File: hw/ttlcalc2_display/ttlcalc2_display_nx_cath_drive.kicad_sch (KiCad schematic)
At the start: 23 parts, among them Q16 MPSA42, Q17 MPSA42, Q18 MPSA42, Q29 MPSA42, Q30 MPSA42, Q31 MPSA42, Q6 MPSA42, Q7 MPSA42, Q8 MPSA42, Q9 MPSA42, U12 74LS42, U7 74LS04, U8 74LS04

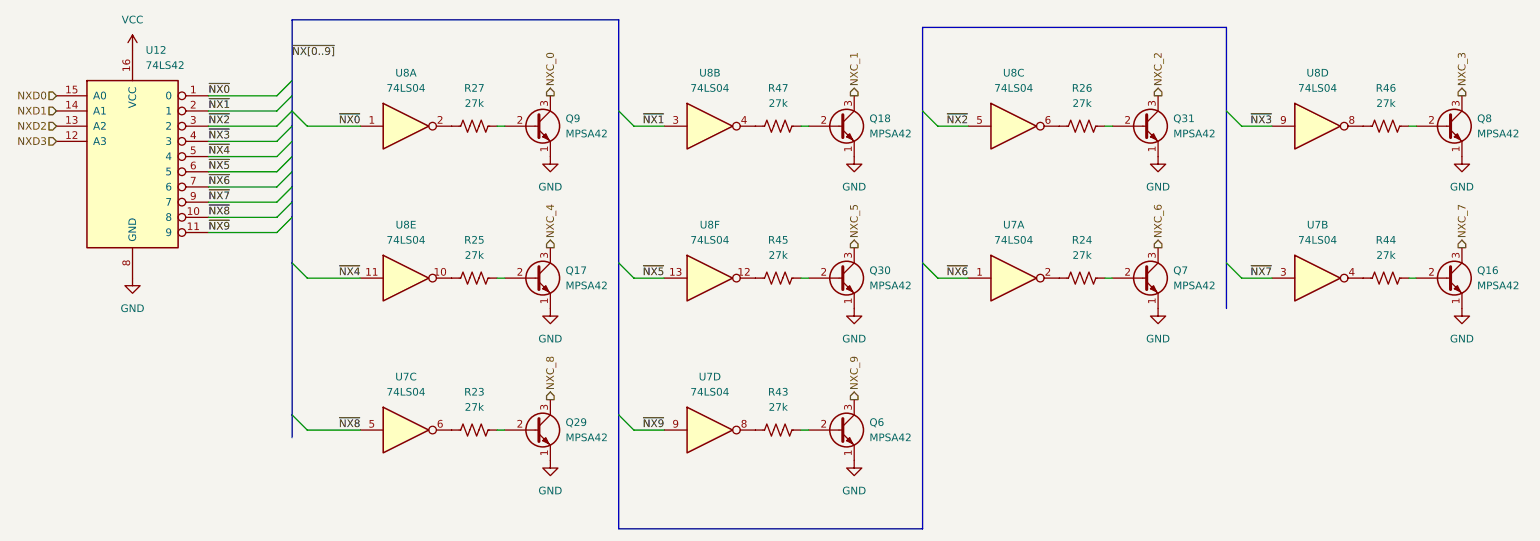
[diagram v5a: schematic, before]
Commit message: Convert to KiCad 9.0
Convert to KiCad 9.0 format
Tweak silkscreen to fix DRC errors introduced by updated footprints
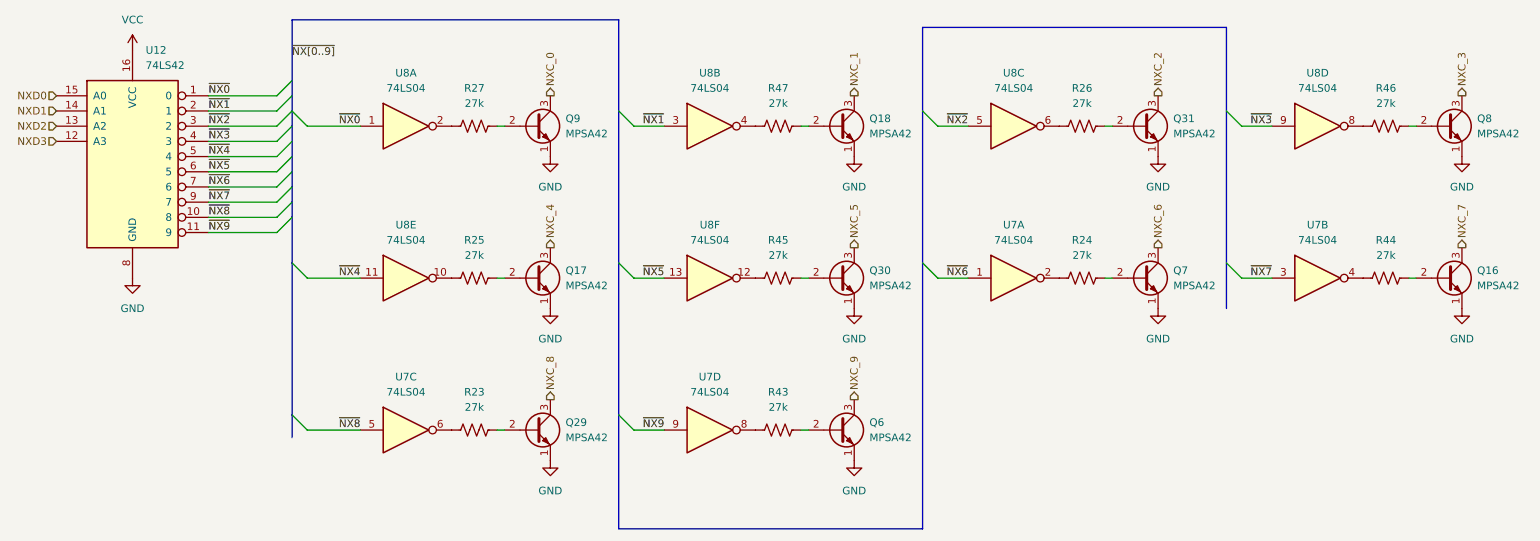
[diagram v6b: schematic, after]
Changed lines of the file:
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@@
 (kicad_sch
-	(version 20231120)
+	(version 20250114)
 	(generator "eeschema")
-	(generator_version "8.0")
+	(generator_version "9.0")
 	(paper "USLetter")
 	(title_block
@@
 	(label "~{NX4}"
 		(at 71.12 66.04 180)
-		(fields_autoplaced yes)
 		(effects
 			(font
@@
 	(label "~{NX7}"
 		(at 45.72 53.34 0)
-		(fields_autoplaced yes)
 		(effects
 			(font
@@
 	(label "~{NX1}"
 		(at 45.72 38.1 0)
-		(fields_autoplaced yes)
 		(effects
 			(font
@@
 	(label "~{NX0}"
 		(at 45.72 35.56 0)
-		(fields_autoplaced yes)
 		(effects
 			(font
@@
 	(label "~{NX6}"
 		(at 172.72 66.04 180)
-		(fields_autoplaced yes)
 		(effects
 			(font
@@
 	(label "~{NX1}"
 		(at 121.92 40.64 180)
-		(fields_autoplaced yes)
 		(effects
 			(font
@@
 	(label "~{NX4}"
 		(at 45.72 45.72 0)
-		(fields_autoplaced yes)
 		(effects
 			(font
@@
 	(label "~{NX5}"
 		(at 121.92 66.04 180)
-		(fields_autoplaced yes)
 		(effects
 			(font
@@
 	(label "~{NX3}"
 		(at 223.52 40.64 180)
-		(fields_autoplaced yes)
 		(effects
 			(font
@@
 	(label "~{NX[0..9]}"
 		(at 59.69 29.21 0)
-		(fields_autoplaced yes)
 		(effects
 			(font
@@
 	(label "~{NX8}"
 		(at 71.12 91.44 180)
-		(fields_autoplaced yes)
 		(effects
 			(font
@@
 	(label "~{NX9}"
 		(at 121.92 91.44 180)
-		(fields_autoplaced yes)
 		(effects
 			(font
@@
 	(label "~{NX9}"
 		(at 45.72 58.42 0)
-		(fields_autoplaced yes)
 		(effects
 			(font
@@
 	(label "~{NX5}"
 		(at 45.72 48.26 0)
-		(fields_autoplaced yes)
 		(effects
 			(font
@@
 	(label "~{NX2}"
 		(at 172.72 40.64 180)
-		(fields_autoplaced yes)
 		(effects
 			(font
@@
 	(label "~{NX7}"
 		(at 223.52 66.04 180)
-		(fields_autoplaced yes)
 		(effects
 			(font
@@
 	(label "~{NX0}"
 		(at 71.12 40.64 180)
-		(fields_autoplaced yes)
 		(effects
 			(font
@@
 	(label "~{NX8}"
 		(at 45.72 55.88 0)
-		(fields_autoplaced yes)
 		(effects
 			(font
@@
 	(label "~{NX2}"
 		(at 45.72 40.64 0)
-		(fields_autoplaced yes)
 		(effects
 			(font
@@
 	(label "~{NX6}"
 		(at 45.72 50.8 0)
-		(fields_autoplaced yes)
 		(effects
 			(font
@@
 	(label "~{NX3}"
 		(at 45.72 43.18 0)
-		(fields_autoplaced yes)
 		(effects
 			(font
@@
 		(shape input)
 		(at 20.32 35.56 180)
-		(fields_autoplaced yes)
 		(effects
 			(font
@@
 		(shape output)
 		(at 255.27 35.56 90)
-		(fields_autoplaced yes)
 		(effects
 			(font
@@
 		(shape output)
 		(at 204.47 60.96 90)
-		(fields_autoplaced yes)
 		(effects
 			(font
@@
 		(shape output)
 		(at 102.87 86.36 90)
-		(fields_autoplaced yes)
 		(effects
 			(font
@@
 		(shape output)
 		(at 102.87 60.96 90)
-		(fields_autoplaced yes)
 		(effects
 			(font
@@
 		(shape output)
 		(at 204.47 35.56 90)
-		(fields_autoplaced yes)
 		(effects
 			(font
@@
 		(shape input)
 		(at 20.32 43.18 180)
-		(fields_autoplaced yes)
 		(effects
 			(font
@@
 		(shape output)
 		(at 153.67 86.36 90)
-		(fields_autoplaced yes)
 		(effects
 			(font
@@
 		(shape output)
 		(at 102.87 35.56 90)
-		(fields_autoplaced yes)
 		(effects
 			(font
@@
 		(shape input)
 		(at 20.32 40.64 180)
-		(fields_autoplaced yes)
 		(effects
 			(font
@@
 		(shape input)
 		(at 20.32 38.1 180)
-		(fields_autoplaced yes)
 		(effects
 			(font
@@
 		(shape output)
 		(at 255.27 60.96 90)
-		(fields_autoplaced yes)
 		(effects
 			(font
@@
 		(shape output)
 		(at 153.67 60.96 90)
-		(fields_autoplaced yes)
 		(effects
 			(font
@@
 		(shape output)
 		(at 153.67 35.56 90)
-		(fields_autoplaced yes)
-		(effects
-			(font
+		(effects
+			(font

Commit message: Minor display hardware revisions
Add anti-ghosting inter-cathode resistors to nixies
Adjust component values based on experiments
Change from individual netclass labels to rule areas
Tweak traces on display board
Update .gitignore to ignore KiCad lock files
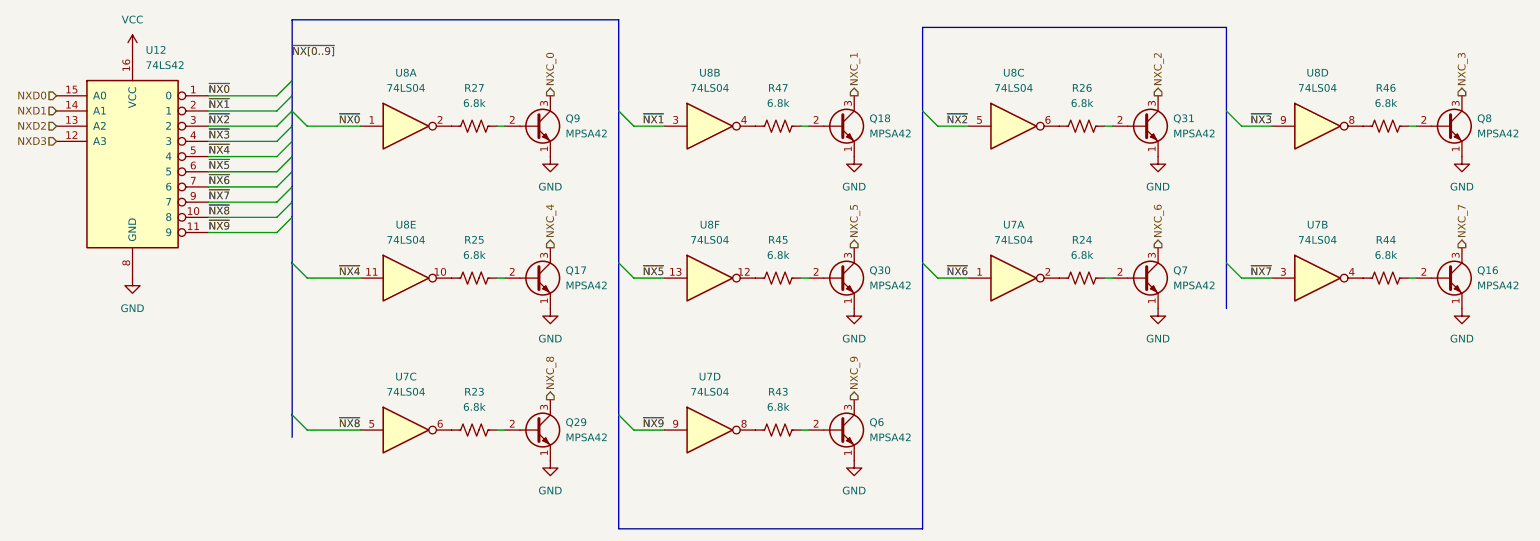
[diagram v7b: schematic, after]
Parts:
- R23, R24, R25, R26, R27, R43, R44, R45, R46, R47: value 27k -> 6.8k
